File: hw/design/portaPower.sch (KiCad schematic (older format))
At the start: 2 parts

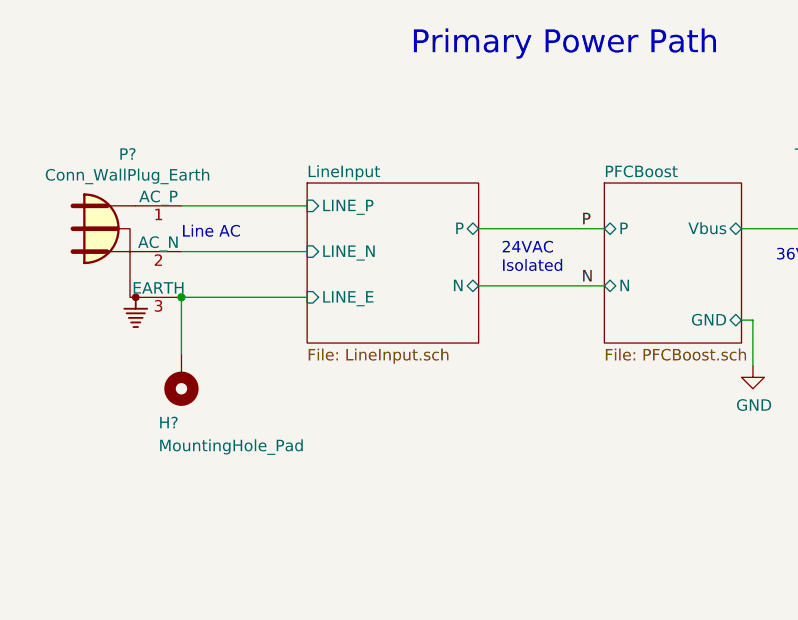
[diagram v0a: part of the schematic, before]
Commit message: updated libraries, new xfmr
updated libraries, selected transformer and added to library/documentation
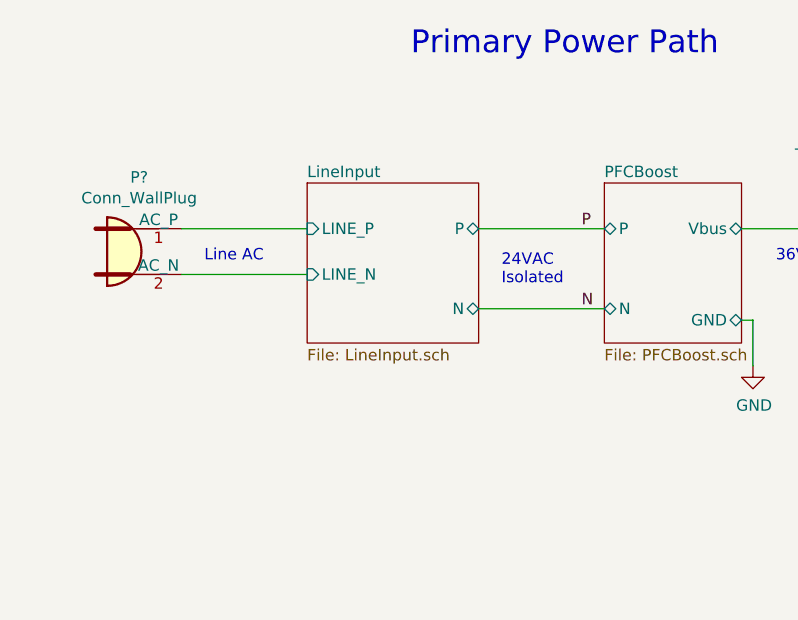
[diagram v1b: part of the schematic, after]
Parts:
- removed H?: MountingHole_Pad, symbol Mechanical:MountingHole_Pad
- removed P?: Conn_WallPlug_Earth, symbol Connector:Conn_WallPlug_Earth
- added P?: Conn_WallPlug, symbol Connector:Conn_WallPlug
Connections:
- net LineInput/LINE_N: now also P?.2 (AC_N)
- net LineInput/LINE_P: now also P?.1 (AC_P)
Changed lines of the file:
@@
 F1 "PFCBoost.sch" 50
 F2 "P" B L 3100 1500 50
-F3 "N" B L 3100 1750 50
+F3 "N" B L 3100 1850 50
 F4 "Vbus" B R 3700 1500 50
 F5 "GND" B R 3700 1900 50
@@
 F0 "LineInput" 50
 F1 "LineInput.sch" 50
-F2 "N" B R 2550 1750 50
+F2 "N" B R 2550 1850 50
 F3 "P" B R 2550 1500 50
-F4 "LINE_P" I L 1800 1400 50
-F5 "LINE_N" I L 1800 1600 50
-F6 "LINE_E" I L 1800 1800 50
-$EndSheet
-Wire Wire Line
-	2550 1750 3100 1750
+F4 "LINE_P" I L 1800 1500 50
+F5 "LINE_N" I L 1800 1700 50
+$EndSheet
+Wire Wire Line
+	2550 1850 3100 1850
 Wire Wire Line
 	2550 1500 3100 1500
-$Comp
-L Connector:Conn_WallPlug_Earth P?
-U 1 1 5E81BB36
-P 950 1500
-F 0 "P?" H 1015 1825 50  0000 C CNN
-F 1 "Conn_WallPlug_Earth" H 1015 1734 50  0000 C CNN
-F 2 "" H 1350 1500 50  0001 C CNN
-F 3 "~" H 1350 1500 50  0001 C CNN
-	1    950  1500
-	1    0    0    -1
-$EndComp
-Wire Wire Line
-	1250 1400 1800 1400
-Wire Wire Line
-	1250 1600 1800 1600
-Wire Wire Line
-	1250 1800 1800 1800
-$Comp
-L Mechanical:MountingHole_Pad H?
-U 1 1 5E81BC25
-P 1250 2150
-F 0 "H?" H 1350 2350 50  0000 R CNN
-F 1 "MountingHole_Pad" H 1350 2450 50  0000 R CNN
-F 2 "" H 1250 2150 50  0001 C CNN
-F 3 "~" H 1250 2150 50  0001 C CNN
-	1    1250 2150
-	-1   0    0    1
-$EndComp
-Wire Wire Line
-	1250 2050 1250 1800
-Connection ~ 1250 1800
+Wire Wire Line
+	1250 1500 1800 1500
 $Comp
 L power:GND #PWR?
@@
 	1    0    0    -1
 $EndComp
-Text Notes 2650 1700 0    50   ~ 0
+Text Notes 2650 1750 0    50   ~ 0
 24VAC\nIsolated
 $Sheet
@@
 F14 "LDO_EN" B R 5150 3600 50
 $EndSheet
-Text Notes 1250 1550 0    50   ~ 0
+Text Notes 1350 1650 0    50   ~ 0
 Line AC
 Wire Wire Line
@@
 Text Label 3000 1500 0    50   ~ 0
 P
-Text Label 3000 1750 0    50   ~ 0
+Text Label 3000 1850 0    50   ~ 0
 N
 $Sheet
@@
 F6 "AuxPG" I L 8000 4700 50
 $EndSheet
+Wire Wire Line
+	1250 1700 1800 1700
+$Comp
+L Connector:Conn_WallPlug P?
+U 1 1 5EC5A887
+P 1050 1600
+F 0 "P?" H 1065 1925 50  0000 C CNN
+F 1 "Conn_WallPlug" H 1065 1834 50  0000 C CNN
+F 2 "" H 1450 1600 50  0001 C CNN
+F 3 "~" H 1450 1600 50  0001 C CNN
+	1    1050 1600
+	1    0    0    -1
+$EndComp
 $EndSCHEMATC

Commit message: more work
more PFC work, more LDO work, added secondary regulator sheet, expanded system power tree sim
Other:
- note added: "Auxiliary Output &\nSecondary Regulators"
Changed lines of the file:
@@
 $Descr A4 11693 8268
 encoding utf-8
-Sheet 1 7
+Sheet 1 8
 Title ""
 Date ""
@@
 F4 "Vadj" B R 5100 1650 50
 F5 "5V" B L 4300 1350 50
-F6 "SYNC" B L 4300 1850 50
-F7 "PGOOD" B L 4300 1750 50
-F8 "Vout" B R 5100 1450 50
+F6 "Vout" B R 5100 1450 50
+F7 "SW_GOOD" B L 4300 1750 50
+F8 "5V_GOOD" B L 4300 1900 50
 $EndSheet
 Wire Wire Line
@@
 Text Label 3000 1850 0    50   ~ 0
 N
-$Sheet
-S 8000 4150 900  800
-U 5EB6CA11
-F0 "AuxOut" 50
-F1 "AuxOut.sch" 50
-F2 "GND" I R 8900 4800 50
-F3 "5VAuxSup" I R 8900 4350 50
-F4 "5VAuxIn" I L 8000 4350 50
-F5 "AuxEN" I L 8000 4550 50
-F6 "AuxPG" I L 8000 4700 50
-$EndSheet
 Wire Wire Line
 	1250 1700 1800 1700
@@
 	1    0    0    -1
 $EndComp
+$Comp
+L power:+5V #PWR?
+U 1 1 5EC498C7
+P 1450 3800
+F 0 "#PWR?" H 1450 3650 50  0001 C CNN
+F 1 "+5V" H 1300 3900 50  0000 C CNN
+F 2 "" H 1450 3800 50  0001 C CNN
+F 3 "" H 1450 3800 50  0001 C CNN
+	1    1450 3800
+	1    0    0    -1
+$EndComp
+Wire Wire Line
+	1450 3800 1450 3900
+Wire Wire Line
+	1450 3900 1700 3900
+$Comp
+L power:GND #PWR?
+U 1 1 5EC49D4C
+P 2700 4600
+F 0 "#PWR?" H 2700 4350 50  0001 C CNN
+F 1 "GND" H 2705 4427 50  0000 C CNN
+F 2 "" H 2700 4600 50  0001 C CNN
+F 3 "" H 2700 4600 50  0001 C CNN
+	1    2700 4600
+	1    0    0    -1
+$EndComp
+Wire Wire Line
+	2700 4600 2700 4400
+Wire Wire Line
+	2700 4400 2600 4400
+Text Notes 1400 3200 0    100  ~ 0
+Auxiliary Output &\nSecondary Regulators
+Wire Wire Line
+	4300 1900 4200 1900
+Wire Wire Line
+	4200 1900 4200 2350
+Wire Wire Line
+	4300 1750 4100 1750
+Wire Wire Line
+	4100 1750 4100 2350
+Text Label 4200 2350 1    50   ~ 0
+PriSW_pg1
+Text Label 4100 2350 1    50   ~ 0
+PriSW_pg2
+$Sheet
+S 1700 5450 900  950
+U 5ECFB146
+F0 "SecRegulators" 50
+F1 "SecRegulators.sch" 50
+F2 "SUP" B L 1700 5650 50
+F3 "GND" B R 2600 6300 50
+F4 "EN" B L 1700 5900 50
+F5 "PGOOD" B L 1700 6150 50
+F6 "3V3" B R 2600 5650 50
+F7 "1V8" B R 2600 5900 50
+$EndSheet
+$Sheet
+S 1700 3750 900  800
+U 5EB6CA11
+F0 "AuxOut" 50
+F1 "AuxOut.sch" 50
+F2 "AuxPOut" B R 2600 3900 50
+F3 "GND" B R 2600 4400 50
+F4 "AuxPIn" B L 1700 3900 50
+F5 "AuxEN" B L 1700 4200 50
+F6 "AuxPG" B L 1700 4350 50
+$EndSheet
 $EndSCHEMATC

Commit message: lots of work
expanded README doc, specifications, added secondary regulator circuit + symbol, more component specs added
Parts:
- added J?: Screw_Terminal_01x02, symbol Connector:Screw_Terminal_01x02
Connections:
- net GND: now also J?.2 (Pin_2)
- net LinearReg/Vload: now also J?.1 (Pin_1)
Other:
- note added: "OUT"
- note added: "OUT + 0.75V"
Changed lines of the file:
@@
 PriSW_pg2
 $Sheet
-S 1700 5450 900  950
+S 1700 5100 900  950
 U 5ECFB146
 F0 "SecRegulators" 50
 F1 "SecRegulators.sch" 50
-F2 "SUP" B L 1700 5650 50
-F3 "GND" B R 2600 6300 50
-F4 "EN" B L 1700 5900 50
-F5 "PGOOD" B L 1700 6150 50
-F6 "3V3" B R 2600 5650 50
-F7 "1V8" B R 2600 5900 50
+F2 "SUP" B L 1700 5300 50
+F3 "GND" B R 2600 5950 50
+F4 "PGOOD" B L 1700 5800 50
+F5 "3V3" B R 2600 5300 50
+F6 "1V8" B R 2600 5550 50
 $EndSheet
 $Sheet
@@
 F6 "AuxPG" B L 1700 4350 50
 $EndSheet
+$Comp
+L power:+5V #PWR?
+U 1 1 5ECAE9D2
+P 1450 5200
+F 0 "#PWR?" H 1450 5050 50  0001 C CNN
+F 1 "+5V" H 1300 5300 50  0000 C CNN
+F 2 "" H 1450 5200 50  0001 C CNN
+F 3 "" H 1450 5200 50  0001 C CNN
+	1    1450 5200
+	1    0    0    -1
+$EndComp
+Wire Wire Line
+	1450 5200 1450 5300
+Wire Wire Line
+	1450 5300 1700 5300
+$Comp
+L power:GND #PWR?
+U 1 1 5ECAF1BA
+P 2700 6150
+F 0 "#PWR?" H 2700 5900 50  0001 C CNN
+F 1 "GND" H 2705 5977 50  0000 C CNN
+F 2 "" H 2700 6150 50  0001 C CNN
+F 3 "" H 2700 6150 50  0001 C CNN
+	1    2700 6150
+	1    0    0    -1
+$EndComp
+Wire Wire Line
+	2700 6150 2700 5950
+Wire Wire Line
+	2700 5950 2600 5950
+Text Notes 5300 1400 0    50   ~ 0
+OUT + 0.75V
+$Comp
+L Connector:Screw_Terminal_01x02 J?
+U 1 1 5ECE72C5
+P 8500 1450
+F 0 "J?" H 8580 1442 50  0000 L CNN
+F 1 "Screw_Terminal_01x02" H 8580 1351 50  0000 L CNN
+F 2 "" H 8500 1450 50  0001 C CNN
+F 3 "~" H 8500 1450 50  0001 C CNN
+	1    8500 1450
+	1    0    0    -1
+$EndComp
+Wire Wire Line
+	8300 1450 6750 1450
+$Comp
+L power:GND #PWR?
+U 1 1 5ECE7CAE
+P 8200 1750
+F 0 "#PWR?" H 8200 1500 50  0001 C CNN
+F 1 "GND" H 8205 1577 50  0000 C CNN
+F 2 "" H 8200 1750 50  0001 C CNN
+F 3 "" H 8200 1750 50  0001 C CNN
+	1    8200 1750
+	1    0    0    -1
+$EndComp
+Wire Wire Line
+	8200 1750 8200 1550
+Wire Wire Line
+	8200 1550 8300 1550
+Text Notes 7550 1350 0    50   ~ 0
+OUT
 $EndSCHEMATC
